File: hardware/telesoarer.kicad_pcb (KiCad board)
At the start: 2 copper layers, 44.2 x 16 mm, 30 parts, among them IC1 ATMEGA328P, K1 RC SIG IN, K2 G T R, P1 ATMEL ISP, P2 PZ, P3 PZ_IN, P4 AOUT, Q1 BC847C, Q2 2N7000, U1 MS5611

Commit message: PCB tweaks
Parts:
- P1: footprint footprints:PIN_ARRAY_3x2_GRUVIN -> POGO_ISP_3x2
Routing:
- net GND: track 127.3 -> 128.0 mm
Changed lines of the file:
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@@
     (thickness 1.6)
     (drawings 27)
-    (tracks 346)
+    (tracks 350)
     (zones 0)
     (modules 30)
@@
   )
   (setup
-    (last_trace_width 0.254)
+    (last_trace_width 0.5)
     (user_trace_width 0.15)
     (user_trace_width 0.254)
@@
     (uvia_drill 0.127)
   )
+  (module POGO_ISP_3x2 (layer F.Cu)
+    (at 54.389 34.155 180)
+    (descr "Double rangee de contacts 2 x 4 pins")
+    (tags CONN)
+    (fp_text reference P1 (at 4.9225 2.151 180) (layer F.SilkS)
+      (effects (font (size 1.016 1.016) (thickness 0.2032)))
+    )
+    (fp_text value "ATMEL ISP" (at 0.7188 6.6722 180) (layer F.SilkS) hide
+      (effects (font (size 1.016 1.016) (thickness 0.2032)))
+    )
+    (fp_line (start 3.81 2.54) (end -3.81 2.54) (layer F.SilkS) (width 0.2032))
+    (fp_line (start -3.81 -2.54) (end 3.81 -2.54) (layer F.SilkS) (width 0.2032))
+    (fp_line (start 3.81 -2.54) (end 3.81 2.54) (layer F.SilkS) (width 0.2032))
+    (fp_line (start -3.81 2.54) (end -3.81 -2.54) (layer F.SilkS) (width 0.2032))
+    (pad 1 smd rect (at -2.54 1.27 180) (size 1.69926 1.89992) (layers F.Cu F.Mask)
+      (net 2 /MISO))
+    (pad 2 smd circle (at -2.54 -1.27 180) (size 1.69926 1.69926) (layers F.Cu F.Mask)
+      (net 1 +5V))
+    (pad 3 smd circle (at 0 1.27 180) (size 1.69926 1.69926) (layers F.Cu F.Mask)
+      (net 5 /SCK))
+    (pad 4 smd circle (at 0 -1.27 180) (size 1.69926 1.69926) (layers F.Cu F.Mask)
+      (net 3 /MOSI))
+    (pad 5 smd circle (at 2.54 1.27 180) (size 1.69926 1.69926) (layers F.Cu F.Mask)
+      (net 4 /RESET))
+    (pad 6 smd circle (at 2.54 -1.27 180) (size 1.69926 1.69926) (layers F.Cu F.Mask)
+      (net 7 GND))
+  )
   (module footprints:C_0603 (layer F.Cu)
     (at 56.388 45.5295 180)
@@
     (tags "resistor 0603")
     (attr smd)
-    (fp_text reference R3 (at -0.1115 -1.135) (layer F.SilkS)
+    (fp_text reference R3 (at 0.3965 -1.135) (layer F.SilkS)
       (effects (font (size 0.508 0.508) (thickness 0.127)))
     )
@@
     )
   )
-  (module footprints:PIN_ARRAY_3x2_GRUVIN (layer F.Cu)
-    (at 54.389 34.155 180)
-    (descr "Double rangee de contacts 2 x 4 pins")
-    (tags CONN)
-    (fp_text reference P1 (at 4.9225 2.151 180) (layer F.SilkS)
-      (effects (font (size 1.016 1.016) (thickness 0.2032)))
-    )
-    (fp_text value "ATMEL ISP" (at 0.7188 6.6722 180) (layer F.SilkS) hide
-      (effects (font (size 1.016 1.016) (thickness 0.2032)))
-    )
-    (fp_line (start 3.81 2.54) (end -3.81 2.54) (layer F.SilkS) (width 0.2032))
-    (fp_line (start -3.81 -2.54) (end 3.81 -2.54) (layer F.SilkS) (width 0.2032))
-    (fp_line (start 3.81 -2.54) (end 3.81 2.54) (layer F.SilkS) (width 0.2032))
-    (fp_line (start -3.81 2.54) (end -3.81 -2.54) (layer F.SilkS) (width 0.2032))
-    (pad 1 smd rect (at -2.54 1.27 180) (size 1.69926 1.89992) (layers F.Cu F.Paste F.Mask)
-      (net 2 /MISO))
-    (pad 2 smd circle (at -2.54 -1.27 180) (size 1.69926 1.69926) (layers F.Cu F.Paste F.Mask)
-      (net 1 +5V))
-    (pad 3 smd circle (at 0 1.27 180) (size 1.69926 1.69926) (layers F.Cu F.Paste F.Mask)
-      (net 5 /SCK))
-    (pad 4 smd circle (at 0 -1.27 180) (size 1.69926 1.69926) (layers F.Cu F.Paste F.Mask)
-      (net 3 /MOSI))
-    (pad 5 smd circle (at 2.54 1.27 180) (size 1.69926 1.69926) (layers F.Cu F.Paste F.Mask)
-      (net 4 /RESET))
-    (pad 6 smd circle (at 2.54 -1.27 180) (size 1.69926 1.69926) (layers F.Cu F.Paste F.Mask)
-      (net 7 GND))
-  )
   (module footprints:SIL-3 (layer F.Cu)
     (at 44.589 40.555 90)
@@
   (gr_line (start 78.6875 35.2545) (end 81.2375 35.2545) (angle 90) (layer F.SilkS) (width 0.15))
   (gr_line (start 78.6875 37.8145) (end 78.6875 35.2545) (angle 90) (layer F.SilkS) (width 0.15))
-  (gr_text github.com/gruvin/telesoarer (at 52.832 31.877 180) (layer B.SilkS)
+  (gr_text github.com/gruvin/telesoarer (at 53.6575 31.877 180) (layer B.SilkS)
     (effects (font (size 0.8 0.8) (thickness 0.15)) (justify mirror))
   )
@@
   (segment (start 67.2465 45.2755) (end 65.913 43.942) (width 0.5) (layer F.Cu) (net 1))
   (segment (start 65.913 43.942) (end 62.23 43.942) (width 0.5) (layer F.Cu) (net 1))
-  (segment (start 61.7855 42.4815) (end 61.425 42.121) (width 0.5) (layer F.Cu) (net 1) (status 2))
+  (segment (start 61.7855 42.4815) (end 61.425 42.121) (width 0.5) (layer F.Cu) (net 1))
   (segment (start 59.225 38.618) (end 58.938 38.618) (width 0.25) (layer F.Cu) (net 2))
   (segment (start 58.938 38.618) (end 57.5945 37.2745) (width 0.25) (layer F.Cu) (net 2))
@@
   (segment (start 57.88025 39.40175) (end 58.039 39.243) (width 0.254) (layer F.Cu) (net 3))
   (segment (start 54.389 35.847) (end 54.389 35.425) (width 0.254) (layer F.Cu) (net 3))
-  (segment (start 47.752 32.0675) (end 47.752 32.9685) (width 0.254) (layer F.Cu) (net 4))
+  (segment (start 48.006 32.8295) (end 47.752 32.9685) (width 0.254) (layer F.Cu) (net 4))
   (segment (start 47.752 32.9685) (end 46.5455 34.175) (width 0.254) (layer F.Cu) (net 4))
   (segment (start 51.889 41.405) (end 51.1145 41.405) (width 0.254) (layer F.Cu) (net 4))
@@
   (segment (start 43.307 44.069) (end 43.307 32.766) (width 0.254) (layer B.Cu) (net 4))
   (segment (start 43.307 32.766) (end 44.0055 32.0675) (width 0.254) (layer B.Cu) (net 4))
-  (segment (start 44.0055 32.0675) (end 47.752 32.0675) (width 0.254) (layer B.Cu) (net 4))
-  (via (at 47.752 32.0675) (size 0.8) (drill 0.4) (layers F.Cu B.Cu) (net 4))
-  (segment (start 47.752 32.0675) (end 51.0315 32.0675) (width 0.254) (layer F.Cu) (net 4))
+  (segment (start 44.0055 32.0675) (end 47.4345 32.0675) (width 0.254) (layer B.Cu) (net 4))
+  (segment (start 47.4345 32.0675) (end 48.006 32.8295) (width 0.254) (layer B.Cu) (net 4))
+  (via (at 48.006 32.8295) (size 0.8) (drill 0.4) (layers F.Cu B.Cu) (net 4))
+  (segment (start 48.006 32.8295) (end 48.7045 32.0675) (width 0.254) (layer F.Cu) (net 4))
+  (segment (start 48.7045 32.0675) (end 51.0315 32.0675) (width 0.254) (layer F.Cu) (net 4))
   (segment (start 51.0315 32.0675) (end 51.849 32.885) (width 0.254) (layer F.Cu) (net 4))
   (segment (start 60.1345 35.433) (end 60.1345 41.91) (width 0.254) (layer B.Cu) (net 5))
@@
   (segment (start 43.929 38.015) (end 44.589 38.015) (width 0.254) (layer F.Cu) (net 6))
   (segment (start 43.827 45.455) (end 43.389 45.017) (width 0.254) (layer F.Cu) (net 6))
+  (segment (start 46.863 32.8295) (end 46.863 33.147) (width 0.5) (layer B.Cu) (net 7))
+  (segment (start 58.943002 33.830498) (end 59.563 33.2105) (width 0.5) (layer B.Cu) (net 7))
+  (segment (start 47.546498 33.830498) (end 58.943002 33.830498) (width 0.5) (layer B.Cu) (net 7))
+  (segment (start 46.863 33.147) (end 47.546498 33.830498) (width 0.5) (layer B.Cu) (net 7))
   (via (at 45.9105 41.4655) (size 0.8) (drill 0.4) (layers F.Cu B.Cu) (net 7))
   (segment (start 45.9105 41.4655) (end 45.974 41.529) (width 0.254) (layer B.Cu) (net 7))
@@
   (segment (start 62.6745 32.5755) (end 64.7065 32.5755) (width 0.5) (layer F.Cu) (net 7))
   (segment (start 61.7855 33.4645) (end 62.6745 32.5755) (width 0.5) (layer F.Cu) (net 7))
-  (segment (start 46.863 32.8295) (end 47.244 33.2105) (width 0.5) (layer B.Cu) (net 7))
-  (segment (start 47.244 33.2105) (end 59.563 33.2105) (width 0.5) (layer B.Cu) (net 7))
   (segment (start 59.563 33.2105) (end 64.0715 33.2105) (width 0.5) (layer B.Cu) (net 7))
   (segment (start 64.0715 33.2105) (end 64.7065 32.5755) (width 0.5) (layer B.Cu) (net 7))

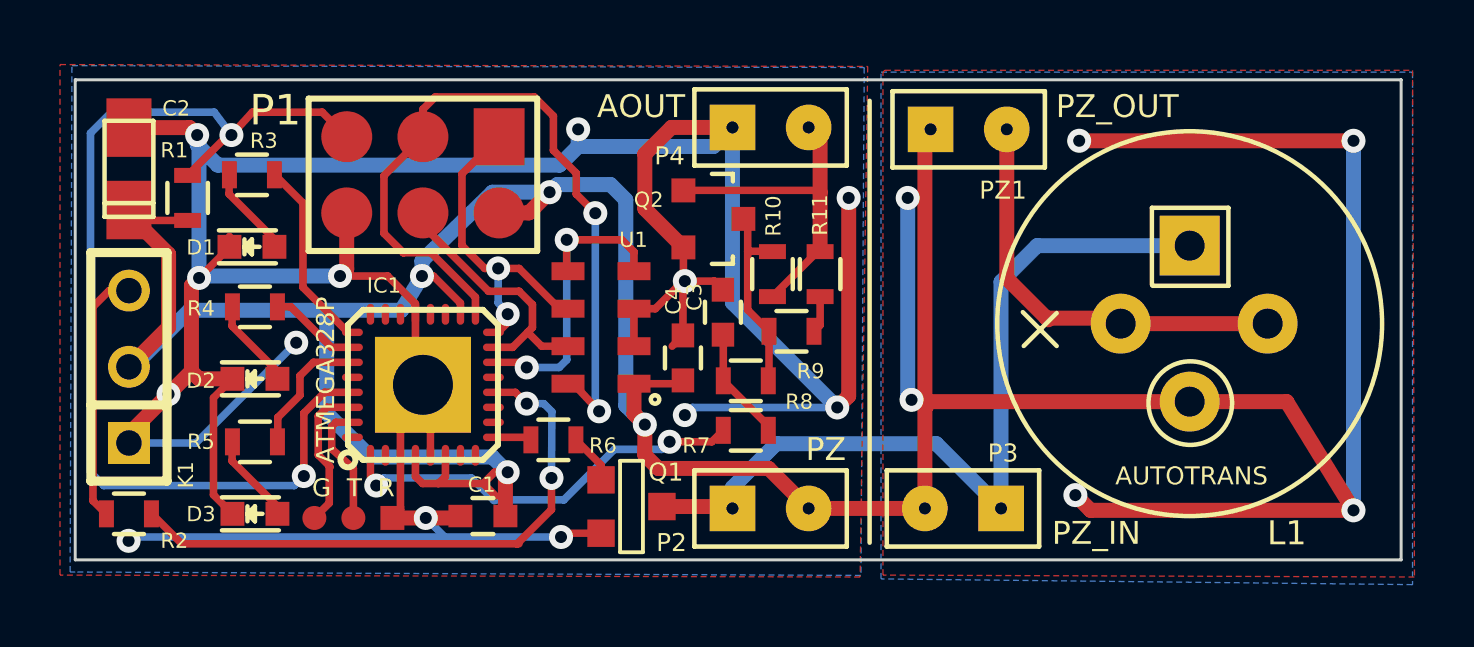
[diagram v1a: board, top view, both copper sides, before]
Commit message: Reduced PCB size.
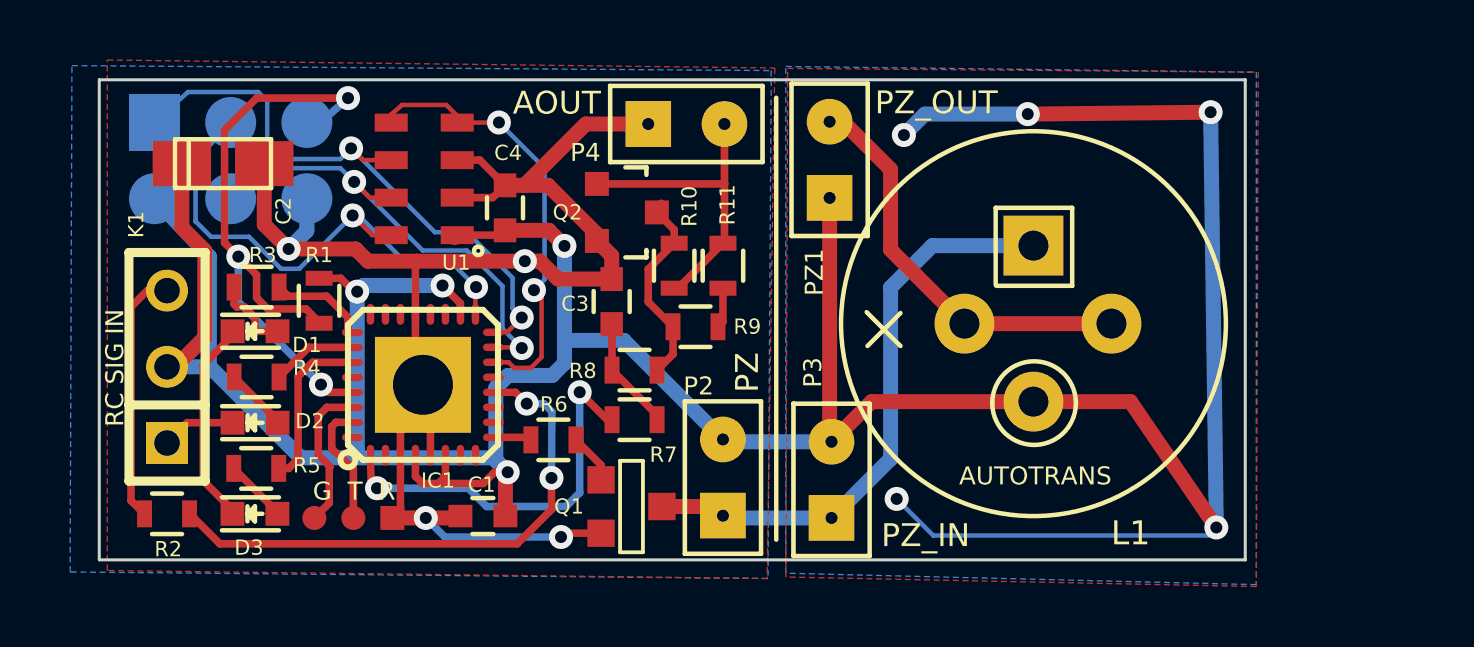
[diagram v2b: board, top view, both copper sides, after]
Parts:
- P1: moved to B.Cu
- moved C4 7.76 mm to (57.1, 35.3)
- moved U1 7.70 mm to (54.4, 34.3)
- moved P1 6.43 mm to (48.0, 33.7), turned to 0 degrees
- moved R1 5.56 mm to (50.9, 38.4), turned to 90 degrees
- moved L1 5.21 mm to (74.7, 39.1)
- moved PZ1 4.75 mm to (67.9, 33.7), turned to 90 degrees
- moved P3 4.48 mm to (68.0, 44.3), turned to 90 degrees
- moved R3 3.75 mm to (48.8, 37.9)
- moved C3 3.73 mm to (60.7, 38.4)
- moved R8 3.73 mm to (61.4, 40.7)
- moved R7 3.73 mm to (61.4, 42.3)
- moved R10 3.29 mm to (62.8, 37.2)
- moved R11 3.25 mm to (64.4, 37.2)
- moved R9 3.20 mm to (63.5, 39.2)
- moved C2 3.14 mm to (47.7, 33.8), turned to 180 degrees
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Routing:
- net GND: track 128.0 -> 61.8 mm, vias 13 -> 4
- net /RESET: track 34.5 -> 21.3 mm, vias 2 -> 3
- net +5V: track 138.7 -> 127.5 mm, vias 10 -> 9
- net /MISO: track 11.0 -> 20.5 mm
- net Net-(L1-Pad1): track 27.9 -> 19.7 mm
- net /SCK: track 25.7 -> 17.8 mm
- net /MOSI: track 8.89 -> 16.2 mm, vias 0 -> 2
- net /~SS: track 10.6 -> 14.7 mm
- net /LED_RED: track 6.26 -> 3.21 mm
- net (no net): track 0.00 -> 2.34 mm
- net Net-(IC1-Pad12): track 19.6 -> 18.3 mm
- net /LED_GREEN: track 4.29 -> 5.38 mm
- net Net-(D2-Pad2): track 3.03 -> 2.12 mm
- net Net-(IC1-Pad1): track 13.9 -> 13.0 mm
- net Net-(D3-Pad2): track 3.03 -> 2.37 mm
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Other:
- board size 44.2 x 16 mm -> 38.2 x 16 mm
- board text added: "Telesoarer v1.0"
- board text added: "github.com/ gruvin/telesoarer"
- board text removed: "Telesoarer Lost Model & Vario Telemetry v1.0"
- board text removed: "github.com/gruvin/telesoarer"

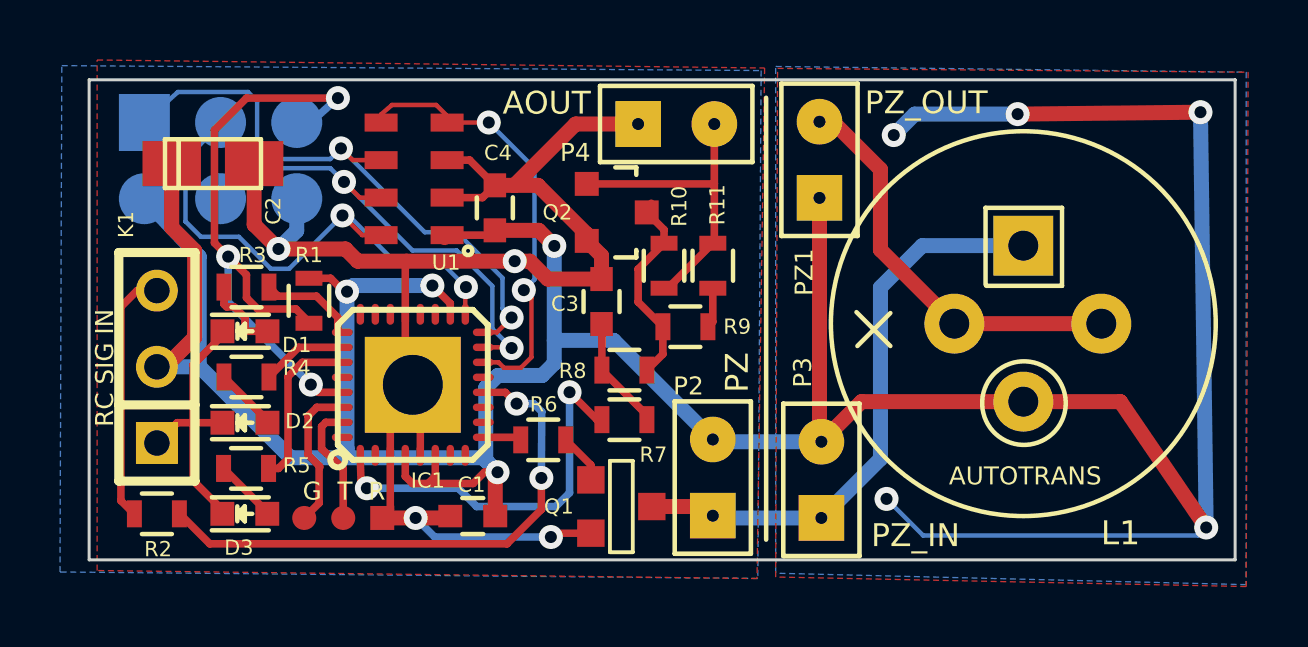
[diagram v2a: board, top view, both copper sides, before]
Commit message: Moved high voltage piezo output away from delicate analog output. Other minor changes.
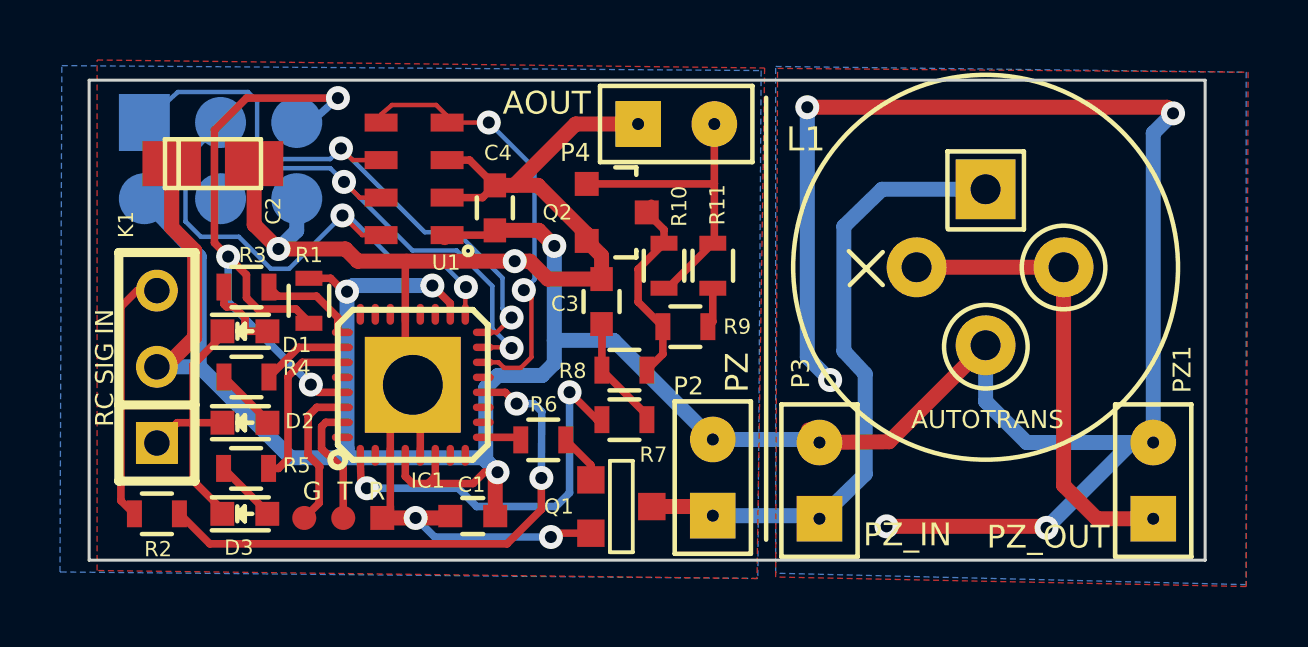
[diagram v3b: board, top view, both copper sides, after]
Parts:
- moved PZ1 15.4 mm to (79.1, 44.3)
- moved L1 2.26 mm to (73.5, 37.2)
- moved P3 0.07 mm to (67.9, 44.3)
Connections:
- PZ1 pad 1: +5V -> Net-(L1-Pad3)
- PZ1 pad 2: Net-(L1-Pad3) -> +5V
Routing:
- net Net-(L1-Pad1): track 19.7 -> 21.8 mm
- net Net-(L1-Pad3): track 14.0 -> 15.6 mm
- net +5V: track 127.5 -> 126.1 mm
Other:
- board size 38.2 x 16 mm -> 37.2 x 16 mm
